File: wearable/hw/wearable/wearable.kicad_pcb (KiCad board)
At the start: 2 copper layers, 0 parts

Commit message: Added 54LDK build
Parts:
- added BT1: 3.7V, Connector_JST:JST_PH_S2B-PH-K_1x02_P2.00mm_Horizontal, F.Cu at (7.42, 24.2)
- added C1: 1uF, Capacitor_SMD:C_0402_1005Metric, F.Cu at (14.7, 0.48)
- added C11: 22uF, Capacitor_SMD:C_0402_1005Metric, F.Cu at (17.6, 4.42)
- added C17: 1uF, Capacitor_SMD:C_0402_1005Metric, F.Cu at (17.6, 6.39)
- added C2: 100uF, Capacitor_SMD:C_0402_1005Metric, F.Cu at (14.7, 2.46)
- added C20: 22uF, Capacitor_SMD:C_0402_1005Metric, F.Cu at (17.6, 8.37)
- added C21: 1uF, Capacitor_SMD:C_0402_1005Metric, F.Cu at (17.6, 10.3)
- added C22: 22uF, Capacitor_SMD:C_0402_1005Metric, F.Cu at (17.6, 12.3)
- added C25: 4.7uF, Capacitor_SMD:C_0402_1005Metric, F.Cu at (20.4, 0.48)
- added C26: 4.7uF, Capacitor_SMD:C_0402_1005Metric, F.Cu at (20.4, 2.46)
- added C27: 1uF, Capacitor_SMD:C_0402_1005Metric, F.Cu at (20.4, 4.42)
- added C28: .1uF, Capacitor_SMD:C_0402_1005Metric, F.Cu at (20.4, 6.39)
- added C29: 1uF, Capacitor_SMD:C_0402_1005Metric, F.Cu at (20.4, 8.37)
- added C3: 1uF, Capacitor_SMD:C_0402_1005Metric, F.Cu at (14.7, 4.42)
- added C30: 1.5nF, Capacitor_SMD:C_0402_1005Metric, F.Cu at (20.4, 10.3)
- added C31: 1uF, Capacitor_SMD:C_0402_1005Metric, F.Cu at (20.4, 12.3)
- added C32: 4.7uF, Capacitor_SMD:C_0402_1005Metric, F.Cu at (23.3, 0.48)
- added C33: 47uF, Capacitor_SMD:C_0402_1005Metric, F.Cu at (23.3, 2.46)
- added C36: 4.7uF, Capacitor_SMD:C_0402_1005Metric, F.Cu at (23.3, 4.42)
- added C37: 100nF, Capacitor_SMD:C_0402_1005Metric, F.Cu at (23.3, 6.39)
- added C38: 22uF, Capacitor_SMD:C_0402_1005Metric, F.Cu at (23.3, 8.37)
- added C39: 10nF, Capacitor_SMD:C_0402_1005Metric, F.Cu at (23.3, 10.3)
- added C4: 0.1uF, Capacitor_SMD:C_0402_1005Metric, F.Cu at (14.7, 6.39)
- added C45: 100nF, Capacitor_SMD:C_0402_1005Metric, F.Cu at (23.3, 12.3)
- added C46: 100nF, Capacitor_SMD:C_0402_1005Metric, F.Cu at (26.2, 0.48)
- added C47: 100nF, Capacitor_SMD:C_0402_1005Metric, F.Cu at (26.2, 2.46)
- added C48: 10uF, Capacitor_SMD:C_0402_1005Metric, F.Cu at (26.2, 4.42)
- added C49: 4.7uF, Capacitor_SMD:C_0402_1005Metric, F.Cu at (26.2, 6.39)
- added C5: 1uF, Capacitor_SMD:C_0402_1005Metric, F.Cu at (14.7, 8.37)
- added C50: 10nF, Capacitor_SMD:C_0402_1005Metric, F.Cu at (26.2, 8.37)
- added C51: 2.2nF, Capacitor_SMD:C_0402_1005Metric, F.Cu at (26.2, 10.3)
- added C52: 2.2nF, Capacitor_SMD:C_0402_1005Metric, F.Cu at (26.2, 12.3)
- added C53: 3.9pF, Capacitor_SMD:C_0402_1005Metric, F.Cu at (29.1, 0.48)
- added C54: 1.5pF, Capacitor_SMD:C_0402_1005Metric, F.Cu at (29.1, 2.46)
- added C55: 2pF, Capacitor_SMD:C_0402_1005Metric, F.Cu at (29.1, 4.42)
- added C56: 0.3pF, Capacitor_SMD:C_0402_1005Metric, F.Cu at (29.1, 6.39)
- added C57: 22pF, Capacitor_SMD:C_0402_1005Metric, F.Cu at (29.1, 8.37)
- added C58: 22pF, Capacitor_SMD:C_0402_1005Metric, F.Cu at (29.1, 10.3)
- added C6: 0.1uF, Capacitor_SMD:C_0402_1005Metric, F.Cu at (14.7, 10.3)
- added C60: 0.1uF, Capacitor_SMD:C_0402_1005Metric, F.Cu at (29.1, 12.3)
- added C7: 1uF, Capacitor_SMD:C_0402_1005Metric, F.Cu at (14.7, 12.3)
- added C8: 10uF, Capacitor_SMD:C_0402_1005Metric, F.Cu at (17.6, 0.48)
- added C9: 0.1uF, Capacitor_SMD:C_0402_1005Metric, F.Cu at (17.6, 2.46)
- added D1: LED, LED_SMD:LED_0402_1005Metric, F.Cu at (25.3, 39.1)
- added D4: LED, LED_SMD:LED_0402_1005Metric, F.Cu at (25.3, 41.1)
- added E1: ~, Connector_PinHeader_1.00mm:PinHeader_1x01_P1.00mm_Horizontal, F.Cu at (32.6, 29.7)
- added E2: ~, Connector_PinHeader_1.00mm:PinHeader_1x01_P1.00mm_Horizontal, F.Cu at (32.6, 32.8)
- added E3: ~, Connector_PinHeader_1.00mm:PinHeader_1x01_P1.00mm_Horizontal, F.Cu at (32.6, 35.8)
- added E4: ~, Connector_PinHeader_1.00mm:PinHeader_1x01_P1.00mm_Horizontal, F.Cu at (32.6, 38.9)
- added E5: ~, Connector_PinHeader_1.00mm:PinHeader_1x01_P1.00mm_Horizontal, F.Cu at (32.6, 41.9)
- added FB1: FerriteBead, Inductor_SMD:L_0201_0603Metric, F.Cu at (28.0, 39.0)
- added H1: ~, ECE445L:MountingHole_4_40, F.Cu at (16.3, 16.4)
- added H2: ~, ECE445L:MountingHole_4_40, F.Cu at (16.3, 22.5)
- added H3: ~, ECE445L:MountingHole_4_40, F.Cu at (16.3, 28.6)
- added H4: ~, ECE445L:MountingHole_4_40, F.Cu at (16.3, 34.7)
- added IC1: LM4041CILPR, ECE445L:ti_LM4041CILPR, F.Cu at (38.0, 24.0)
- added J1: Analog, Connector_PinHeader_2.54mm:PinHeader_1x03_P2.54mm_Vertical, F.Cu at (39.1, 30.5)
- added J2: Conn_02x05_Odd_Even, Connector_PinHeader_1.27mm:PinHeader_2x05_P1.27mm_Vertical_SMD, F.Cu at (35.3, 3.71)
- added J3: Interrupts, Connector_PinHeader_2.54mm:PinHeader_1x08_P2.54mm_Vertical, F.Cu at (1.79, 1.79)
- added J4: Data, Connector_PinHeader_2.54mm:PinHeader_1x08_P2.54mm_Vertical, F.Cu at (6.38, 1.79)
- added J5: Data, Connector_PinHeader_2.54mm:PinHeader_1x02_P2.54mm_Vertical, F.Cu at (36.6, 15.6)
- added J8: USBC Charger, Connector_PinHeader_2.54mm:PinHeader_1x08_P2.54mm_Vertical, F.Cu at (11.0, 1.79)
- added L1: 1.5uH, Inductor_SMD:L_1008_2520Metric, F.Cu at (1.98, 23.7)
- added L2: 4.7nH, Inductor_SMD:L_1008_2520Metric, F.Cu at (1.98, 27.5)
- added L5: 2.7nH, Inductor_SMD:L_1008_2520Metric, F.Cu at (1.98, 31.2)
- added L6: 3.5nH, Inductor_SMD:L_1008_2520Metric, F.Cu at (1.98, 35.0)
- added L7: 2.7nH, Inductor_SMD:L_1008_2520Metric, F.Cu at (1.98, 38.7)
- added R1: 5.1K, Resistor_SMD:R_0402_1005Metric, F.Cu at (20.9, 29.2)
- added R10: 499, Resistor_SMD:R_0402_1005Metric, F.Cu at (23.8, 37.2)
- added R11: 453K, Resistor_SMD:R_0402_1005Metric, F.Cu at (26.7, 29.2)
- added R12: 10K, Resistor_SMD:R_0402_1005Metric, F.Cu at (26.7, 31.2)
- added R13: 10K, Resistor_SMD:R_0402_1005Metric, F.Cu at (26.7, 33.2)
- added R14: 10K, Resistor_SMD:R_0402_1005Metric, F.Cu at (26.7, 35.2)
- added R15: 10K, Resistor_SMD:R_0402_1005Metric, F.Cu at (26.7, 37.2)
- added R16: 49.9K, Resistor_SMD:R_0402_1005Metric, F.Cu at (29.6, 29.2)
- added R17: 49.9K, Resistor_SMD:R_0402_1005Metric, F.Cu at (29.6, 31.2)
- added R18: 10K, Resistor_SMD:R_0402_1005Metric, F.Cu at (29.6, 33.2)
- added R19: 10K, Resistor_SMD:R_0402_1005Metric, F.Cu at (29.6, 35.2)
- added R2: 1M, Resistor_SMD:R_0402_1005Metric, F.Cu at (20.9, 31.2)
- added R22: 10K, Resistor_SMD:R_0402_1005Metric, F.Cu at (29.6, 37.2)
- added R3: 100K, Resistor_SMD:R_0402_1005Metric, F.Cu at (20.9, 33.2)
- added R4: 100K, Resistor_SMD:R_0402_1005Metric, F.Cu at (20.9, 35.2)
- added R5: 330, Resistor_SMD:R_0402_1005Metric, F.Cu at (20.9, 37.2)
- added R6: 820, Resistor_SMD:R_0402_1005Metric, F.Cu at (23.8, 29.2)
- added R7: 10k, Resistor_SMD:R_0402_1005Metric, F.Cu at (23.8, 31.2)
- added R8: 10k, Resistor_SMD:R_0402_1005Metric, F.Cu at (23.8, 33.2)
- added R9: 200K, Resistor_SMD:R_0402_1005Metric, F.Cu at (23.8, 35.2)
- added SW1: SW_Toggle, Connector_PinHeader_2.54mm:PinHeader_1x02_P2.54mm_Vertical, F.Cu at (41.2, 15.6)
- added U1: LT3042xMSE, Package_SO:MSOP-10-1EP_3x3mm_P0.5mm_EP1.68x1.88mm, F.Cu at (34.1, 10.2)
- added U2: BNO080, BNO080:IC_BNO080, F.Cu at (40.2, 40.9)
- added U3: nRF54L15-QFXX, Package_DFN_QFN:QFN-48-1EP_6x6mm_P0.4mm_EP4.6x4.6mm, F.Cu at (8.95, 35.6)
- added U4: MAX77659AENV+, MAX77659AENV+:21-100509_N302D2&plus_1_MXM, F.Cu at (21.5, 40.2)
- added U5: ADS1299IPAG, ADS1299:PAG64_TEX, F.Cu at (26.9, 20.7)
- added Y1: 32MHz, Unknown:Crystal_SMD_2016-2Pin_2.0x1.6mm, F.Cu at (42.1, 1.12)
- added Y2: 32.768kHz, Crystal:Crystal_SMD_2012-2Pin_2.0x1.2mm, F.Cu at (42.1, 4.38)
- added Y3: 32.768kHz, Crystal:Crystal_SMD_3215-2Pin_3.2x1.5mm, F.Cu at (40.3, 9.59)

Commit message: Started early version of layout
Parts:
- moved J3 153.8 mm to (101.1, 119.2), turned to -90 degrees
- moved J4 145.3 mm to (101.4, 111.8), turned to -90 degrees
- moved BT1 133.1 mm to (125.5, 85.8), turned to -90 degrees
- moved J2 128.6 mm to (123.0, 97.7)
- moved R10 121.9 mm to (138.3, 78.7)
- moved R11 121.9 mm to (141.2, 70.8)
- moved R3 121.9 mm to (135.4, 74.8)
- moved R4 121.9 mm to (135.4, 76.8)
- moved R5 121.9 mm to (135.4, 78.7)
- moved R6 121.9 mm to (138.3, 70.8)
- moved R7 121.9 mm to (138.3, 72.8)
- moved R8 121.9 mm to (138.3, 74.8)
- moved R9 121.9 mm to (138.3, 76.8)
- moved R16 121.9 mm to (144.2, 70.8)
- moved R17 121.9 mm to (144.2, 72.8)
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
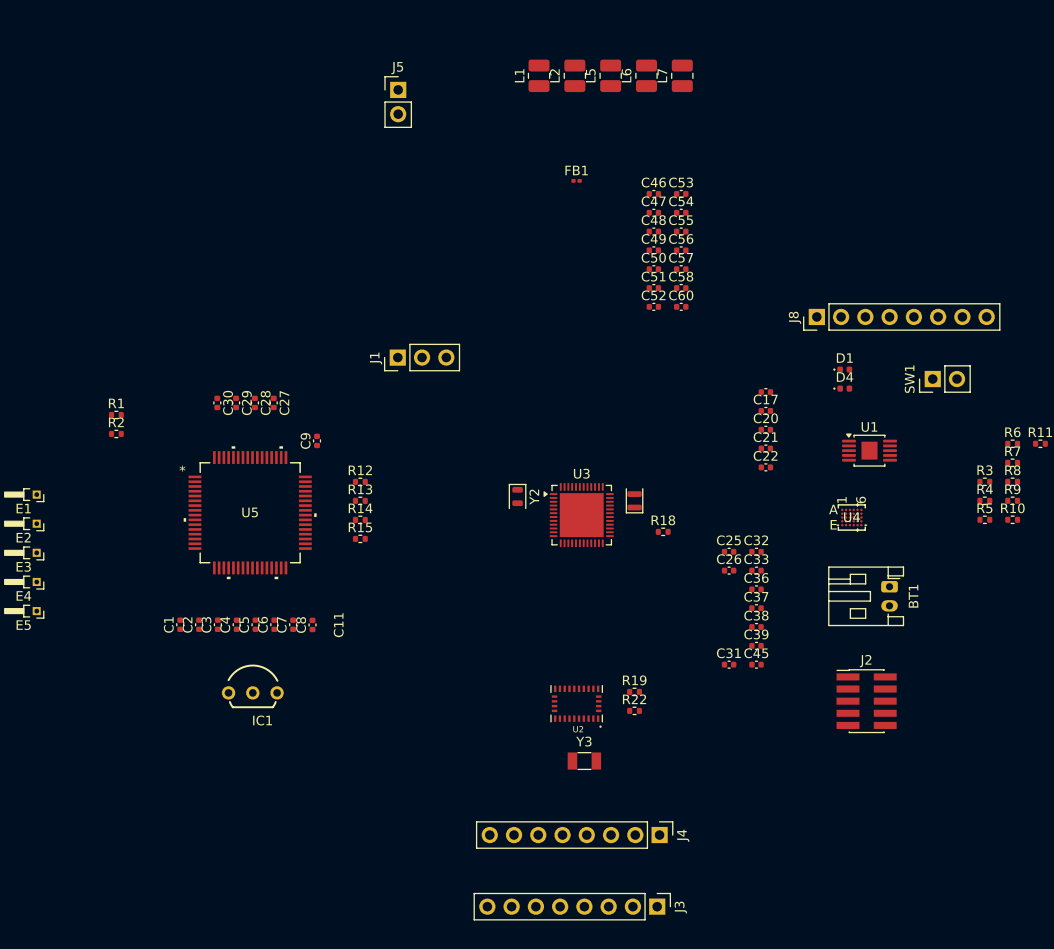
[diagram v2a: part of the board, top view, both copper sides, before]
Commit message: Starting to layout nrf54L15
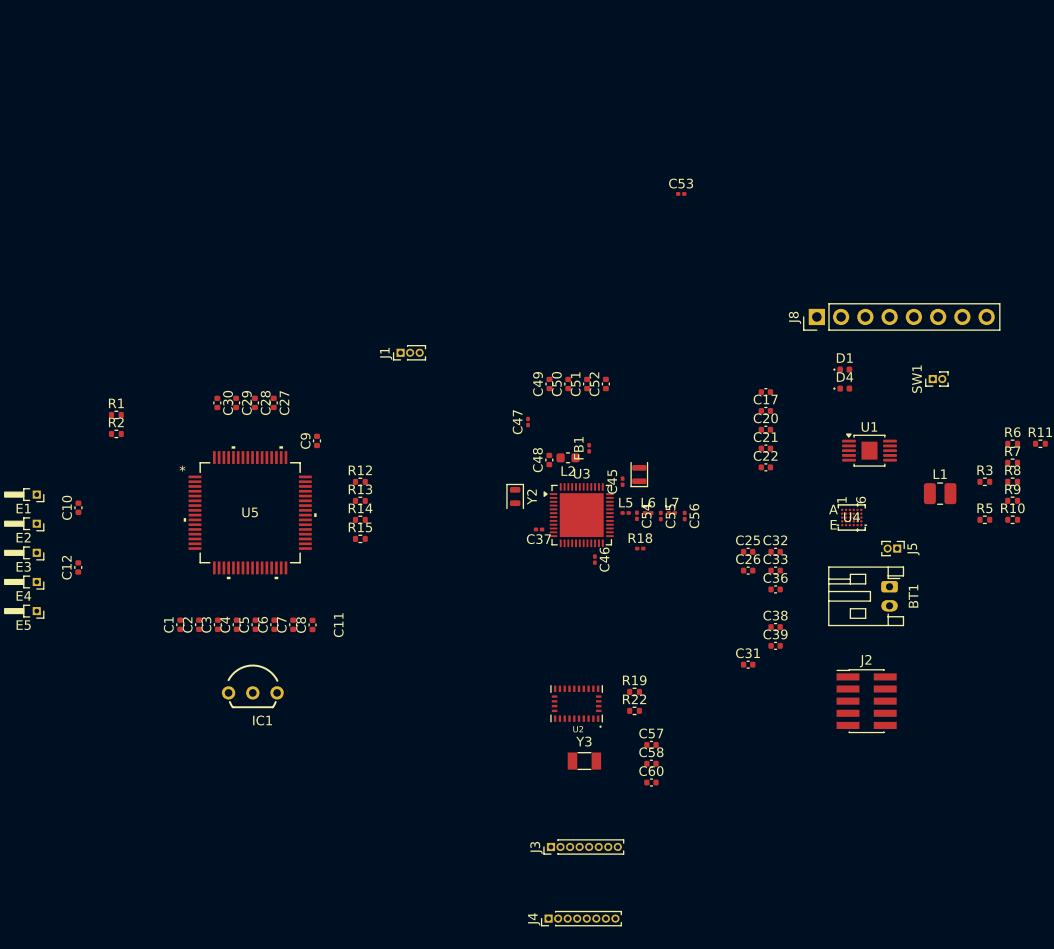
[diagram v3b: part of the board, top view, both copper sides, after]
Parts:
- removed R4: 100K, Resistor_SMD:R_0402_1005Metric
- added C10: ???, Capacitor_SMD:C_0402_1005Metric, F.Cu at (40.5, 77.5)
- added C12: ???, Capacitor_SMD:C_0402_1005Metric, F.Cu at (40.5, 83.7)
- C37, C45, C46, C47, C53, C54, C55, C56: footprint Capacitor_SMD:C_0402_1005Metric -> Capacitor_SMD:C_0201_0603Metric
- J1: footprint Connector_PinHeader_2.54mm:PinHeader_1x03_P2.54mm_Vertical -> Connector_PinHeader_1.00mm:PinHeader_1x03_P1.00mm_Vertical
- J3, J4: footprint Connector_PinHeader_2.54mm:PinHeader_1x08_P2.54mm_Vertical -> Connector_PinHeader_1.00mm:PinHeader_1x08_P1.00mm_Vertical
- J5, SW1: footprint Connector_PinHeader_2.54mm:PinHeader_1x02_P2.54mm_Vertical -> Connector_PinHeader_1.00mm:PinHeader_1x02_P1.00mm_Vertical
- L2: footprint Inductor_SMD:L_1008_2520Metric -> Inductor_SMD:L_0603_1608Metric
- L5, L6, L7: footprint Inductor_SMD:L_1008_2520Metric -> Inductor_SMD:L_0201_0603Metric
- R18: footprint Resistor_SMD:R_0402_1005Metric -> Resistor_SMD:R_0201_0603Metric
- moved J5 71.0 mm to (126.2, 81.8), turned to -90 degrees
- moved L1 60.6 mm to (130.8, 76.0), turned to 0 degrees
- moved C57 49.9 mm to (100.5, 102.3)
- moved C58 49.9 mm to (100.5, 104.3)
- moved C60 49.9 mm to (100.5, 106.2)
- moved L5 45.8 mm to (97.8, 78.0), turned to 0 degrees
- moved L7 45.8 mm to (102.7, 78.0), turned to 0 degrees
- moved L6 45.8 mm to (100.2, 78.0), turned to 0 degrees
- moved L2 40.0 mm to (91.8, 72.2), turned to 180 degrees
- moved C46 38.8 mm to (94.6, 82.9), turned to -90 degrees
- moved C54 32.1 mm to (99.0, 78.3), turned to -90 degrees
- moved C55 29.9 mm to (101.5, 78.3), turned to -90 degrees
- moved FB1 28.0 mm to (94.0, 71.2), turned to 90 degrees
- moved C56 27.8 mm to (104.0, 78.3), turned to -90 degrees
- moved C48 26.3 mm to (89.8, 72.5), turned to 90 degrees
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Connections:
- C30 pad 2: Net-(C30-Pad2) -> Net-(U5-BIASINV)
- C53 pad 1: Net-(U3-~{RESET}) -> RESET
- E5 pad 1: Net-(C30-Pad2) -> Net-(U5-BIASIN)
- R18 pad 1: Net-(U3-~{RESET}) -> RESET
- R18 pad 2: RESET -> +3V3
- R2 pad 2: Net-(C30-Pad2) -> Net-(U5-BIASINV)
- U3 pad 30: Net-(U3-~{RESET}) -> RESET
- U4 pad B5: nRST -> RESET
- U5 pad 61: unconnected-(U5-BIASINV-Pad61) -> Net-(U5-BIASINV)

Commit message: Placed a bunch of stuff
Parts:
- added R20: 10K, Resistor_SMD:R_0201_0603Metric, F.Cu at (52.9, 72.5)
- added R21: 10K, Resistor_SMD:R_0201_0603Metric, F.Cu at (52.9, 79.0)
- added R23: 10K, Resistor_SMD:R_0201_0603Metric, F.Cu at (52.9, 80.8)
- added R4: 10K, Resistor_SMD:R_0201_0603Metric, F.Cu at (52.9, 74.8)
- added TP1: BatteryStatus, TestPoint:TestPoint_Bridge_Pitch2.0mm_Drill0.7mm, F.Cu at (108.8, 74.8)
- C10, C12: value ??? -> 4.7nF
- C49: value 4.7uF -> 2.2uF; footprint Capacitor_SMD:C_0402_1005Metric -> Capacitor_SMD:C_0201_0603Metric
- C50, C51, C52: footprint Capacitor_SMD:C_0402_1005Metric -> Capacitor_SMD:C_0201_0603Metric
- J1: value Analog -> Data; footprint Connector_PinHeader_1.00mm:PinHeader_1x03_P1.00mm_Vertical -> Connector_PinHeader_1.00mm:PinHeader_1x02_P1.00mm_Vertical
- L1: footprint Inductor_SMD:L_1008_2520Metric -> Capacitor_SMD:C_0201_0603Metric
- moved H4 138.7 mm to (143.2, 93.0)
- moved H3 131.0 mm to (143.2, 62.5)
- moved H2 73.7 mm to (46.0, 93.5)
- moved J1 58.3 mm to (131.0, 74.8)
- moved J4 56.7 mm to (94.0, 64.0)
- moved H1 52.1 mm to (46.0, 62.5)
- moved J3 49.4 mm to (83.5, 64.0)
- moved C53 36.6 mm to (98.6, 80.8)
- moved R1 32.2 mm to (73.0, 82.8)
- moved SW1 28.9 mm to (138.0, 91.8), turned to 0 degrees
- moved C36 27.6 mm to (132.7, 66.2), turned to 90 degrees
- moved C58 26.2 mm to (82.7, 85.0)
- moved J8 26.0 mm to (141.5, 68.4), turned to 0 degrees
- moved C26 24.1 mm to (131.5, 72.0)
- moved R6 22.5 mm to (116.8, 64.5), turned to -90 degrees
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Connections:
- E1 pad 1: Net-(U5-IN2N) -> Net-(E1-Pad1)
- E2 pad 1: Net-(U5-IN2P) -> Net-(E2-Pad1)
- E3 pad 1: Net-(U5-IN1N) -> Net-(E3-Pad1)
- E4 pad 1: Net-(U5-IN1P) -> Net-(E4-Pad1)
- J4 pad 4: CS_ADS1299 -> CS_BNO085
- J4 pad 5: CS_BNO085 -> CS_ADS1299
- J4 pad 6: SCL -> DRDY
- J4 pad 7: SDA -> SCL
- J4 pad 8: DRDY -> SDA

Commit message: Getting there
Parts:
- removed J1: Data, Connector_PinHeader_1.00mm:PinHeader_1x02_P1.00mm_Vertical
- added TP2: AVSS, TestPoint:TestPoint_Bridge_Pitch2.0mm_Drill0.7mm, F.Cu at (103.8, 62.8)
- added TP3: AVDD, TestPoint:TestPoint_Bridge_Pitch2.0mm_Drill0.7mm, F.Cu at (109.0, 62.8)
- C37, C45, C46, C47, C49, C50, C51, C52, C53, C54, C55, C56: footprint Capacitor_SMD:C_0201_0603Metric -> Capacitor_SMD:C_0402_1005Metric
- FB1, L5, L6, L7: footprint Inductor_SMD:L_0201_0603Metric -> Inductor_SMD:L_0402_1005Metric_Pad0.77x0.64mm_HandSolder
- L1: footprint Capacitor_SMD:C_0201_0603Metric -> Inductor_SMD:L_0402_1005Metric_Pad0.77x0.64mm_HandSolder
- R18, R20, R21, R23, R4: footprint Resistor_SMD:R_0201_0603Metric -> Resistor_SMD:R_0402_1005Metric
- moved J5 40.0 mm to (94.5, 62.8), turned to 90 degrees
- moved SW1 25.4 mm to (121.8, 72.2)
- moved C26 19.3 mm to (112.2, 72.2), turned to -90 degrees
- moved C25 18.2 mm to (105.0, 66.8)
- moved R9 18.2 mm to (102.7, 69.5)
- moved U1 18.2 mm to (107.1, 69.3)
- moved C36 18.0 mm to (114.7, 66.8)
- moved R11 18.0 mm to (112.2, 69.5)
- moved R16 18.0 mm to (114.7, 69.5)
- moved R17 18.0 mm to (112.2, 66.8)
- moved R10 16.2 mm to (106.4, 72.5)
- moved H3 16.1 mm to (127.2, 64.2)
- moved J8 16.0 mm to (125.5, 69.4)
- moved H4 16.0 mm to (127.2, 92.5)
- moved TP1 15.8 mm to (98.5, 62.8)
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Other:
- board outline added: 83.5 x 35 mm

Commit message: More layout progress and some fun stuff
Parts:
- added G***: LOGO, LOGO, F.Cu at (130.6, 116.8)
- added G***: LOGO, LOGO, F.Cu at (125.1, 116.8)
- TP1: value BatteryStatus -> AVDD
- TP3: value AVDD -> BatteryStatus
- moved TP1 74.5 mm to (167.3, 91.2)
- moved TP2 74.5 mm to (172.6, 91.2)
- moved TP3 74.5 mm to (177.8, 91.2)
- moved C11 71.9 mm to (180.5, 107.2)
- moved C17 71.9 mm to (184.8, 102.2)
- moved C20 71.9 mm to (183.8, 108.3)
- moved C21 71.9 mm to (185.2, 108.3)
- moved C22 71.9 mm to (187.4, 106.0)
- moved C25 71.9 mm to (171.2, 95.0)
- moved C26 71.9 mm to (178.4, 100.5)
- moved C31 71.9 mm to (183.2, 102.2)
- moved C32 71.9 mm to (180.5, 103.2)
- moved C33 71.9 mm to (180.5, 105.9)
- moved C36 71.9 mm to (180.9, 95.0)
- moved C39 71.9 mm to (182.4, 108.3)
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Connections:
- TP1 pad 1: AMUX -> AVDD
- TP3 pad 1: AVDD -> AMUX
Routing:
- net Net-(U5-VREFP): track 0.00 -> 8.01 mm
- net AVSS: track 0.00 -> 6.88 mm
- net Net-(U1-SET): track 0.00 -> 6.78 mm
- net +3V3: track 0.00 -> 6.45 mm
- net Net-(U3-DECA): track 0.00 -> 6.37 mm
- net Net-(U1-PGFB): track 0.00 -> 6.01 mm
- net Net-(U5-GPIO1): track 0.00 -> 5.40 mm
- net /XIN: track 0.00 -> 5.15 mm
- net /XOUT: track 0.00 -> 5.10 mm
- net Net-(U5-VCAP2): track 0.00 -> 4.80 mm
- net Net-(U5-VCAP1): track 0.00 -> 4.59 mm
- net Net-(U5-VCAP3): track 0.00 -> 4.45 mm
- net Net-(U5-GPIO2): track 0.00 -> 4.44 mm
- net Net-(U3-DCC): track 0.00 -> 4.41 mm
- net Net-(U5-VCAP4): track 0.00 -> 4.38 mm
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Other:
- board size 83.5 x 35 mm -> 80.2 x 35 mm
- board text added: "ECE 464K: Aidan Aalund, Justin Bahn, Alex Ho, Kien Ton"
- board text added: "Snoozy"

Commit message: Some more changes
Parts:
- moved C54 0.45 mm to (158.8, 102.5)
- moved C56 0.42 mm to (165.8, 102.5)
- moved C55 0.41 mm to (162.3, 102.5)
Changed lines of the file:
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@@
 	(footprint "Capacitor_SMD:C_0402_1005Metric"
 		(layer "F.Cu")
-		(at 158.7775 102.07 -90)
+		(at 158.7775 102.52 -90)
 		(descr "Capacitor SMD 0402 (1005 Metric), square (rectangular) end terminal, IPC-7351 nominal, (Body size source: IPC-SM-782 page 76, https://www.pcb-3d.com/wordpress/wp-content/uploads/ipc-sm-782a_amendment_1_and_2.pdf), generated with kicad-footprint-generator")
 		(tags "capacitor")
@@
 	(footprint "Capacitor_SMD:C_0402_1005Metric"
 		(layer "F.Cu")
-		(at 165.7775 102.095 -90)
+		(at 165.7775 102.52 -90)
 		(descr "Capacitor SMD 0402 (1005 Metric), square (rectangular) end terminal, IPC-7351 nominal, (Body size source: IPC-SM-782 page 76, https://www.pcb-3d.com/wordpress/wp-content/uploads/ipc-sm-782a_amendment_1_and_2.pdf), generated with kicad-footprint-generator")
 		(tags "capacitor")
@@
 	(footprint "Capacitor_SMD:C_0402_1005Metric"
 		(layer "F.Cu")
-		(at 162.2775 102.095 -90)
+		(at 162.2775 102.5 -90)
 		(descr "Capacitor SMD 0402 (1005 Metric), square (rectangular) end terminal, IPC-7351 nominal, (Body size source: IPC-SM-782 page 76, https://www.pcb-3d.com/wordpress/wp-content/uploads/ipc-sm-782a_amendment_1_and_2.pdf), generated with kicad-footprint-generator")
 		(tags "capacitor")
@@
 		(layer "F.Cu")
 		(net 1)
+	)
+	(segment
+		(start 165.7575 102.98)
+		(end 165.7775 103)
+		(width 0.5)
+		(layer "F.Cu")
+		(net 1)

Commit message: Some stuff
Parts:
- moved C56 0.22 mm to (166.0, 102.5)
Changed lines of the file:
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@@
 	(footprint "Capacitor_SMD:C_0402_1005Metric"
 		(layer "F.Cu")
-		(at 165.7775 102.52 -90)
+		(at 166 102.5 -90)
 		(descr "Capacitor SMD 0402 (1005 Metric), square (rectangular) end terminal, IPC-7351 nominal, (Body size source: IPC-SM-782 page 76, https://www.pcb-3d.com/wordpress/wp-content/uploads/ipc-sm-782a_amendment_1_and_2.pdf), generated with kicad-footprint-generator")
 		(tags "capacitor")
@@
 		(layer "F.Cu")
 		(net 1)
-	)
-	(segment
-		(start 165.7575 102.98)
-		(end 165.7775 103)
-		(width 0.5)
-		(layer "F.Cu")
-		(net 1)
